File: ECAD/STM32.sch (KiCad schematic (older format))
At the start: 13 parts, among them J4 Conn_02x03_Odd_Even, U1 STM32F072C8Ux, U2 STM32F071C8Tx

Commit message: routing almost done
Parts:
- removed U2: STM32F071C8Tx, Package_QFP:LQFP-48_7x7mm_P0.5mm, symbol MCU_ST_STM32F0:STM32F071C8Tx
- C2, C3, C4, C7, C8: renamed from C?; symbol Device:C -> OtterIronProRedesign-rescue:C-Device
- C5: renamed from C3; symbol Device:C -> OtterIronProRedesign-rescue:C-Device
- C6: renamed from C4; symbol Device:C -> OtterIronProRedesign-rescue:C-Device
- J23: renamed from J4; symbol Connector_Generic:Conn_02x03_Odd_Even -> OtterIronProRedesign-rescue:Conn_02x03_Odd_Even-Connector_Generic
- NT1: renamed from NT9; symbol Device:Net-Tie_2 -> OtterIronProRedesign-rescue:Net-Tie_2-Device
- NT2: renamed from NT10; symbol Device:Net-Tie_2 -> OtterIronProRedesign-rescue:Net-Tie_2-Device
- R7: renamed from R6; symbol Device:R -> OtterIronProRedesign-rescue:R-Device
- U1: symbol MCU_ST_STM32F0:STM32F072C8Ux -> OtterIronProRedesign-rescue:STM32F072C8Ux-MCU_ST_STM32F0
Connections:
- net CurrentMeasurement: now also U1.11 (PA1); no longer U1.10 (PA0)
- net I2C_SCL: now also U1.21 (PB10); no longer U1.42 (PB6)
- net I2C_SDA: now also U1.22 (PB11); no longer U1.43 (PB7)
- net IronTemperature: now also U1.12 (PA2); no longer U1.11 (PA1)
- net PcbTemperature: now also U1.13 (PA3); no longer U1.15 (PA5)
- net Switch1: now also U1.26 (PB13); no longer U1.13 (PA3)
- net Switch2: now also U1.3 (PC14); no longer U1.2 (PC13)
- net USB_Alert: now also U1.27 (PB14); no longer U1.25 (PB12)
- net VBusMeasurement: now also U1.10 (PA0); no longer U1.12 (PA2)
- net ~VBusAvailable: now also U1.25 (PB12)
- net IronPwmH: now reaches U1.45 (PB8)
- net IronPwm: no longer names the net of U1.29 (PA8)
- new net IronPwmL: U1.42 (PB6)
- no-connect marks 46 -> 21
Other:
- note added: "TIM16_CH1"
- note added: "TIM16_CH1N"

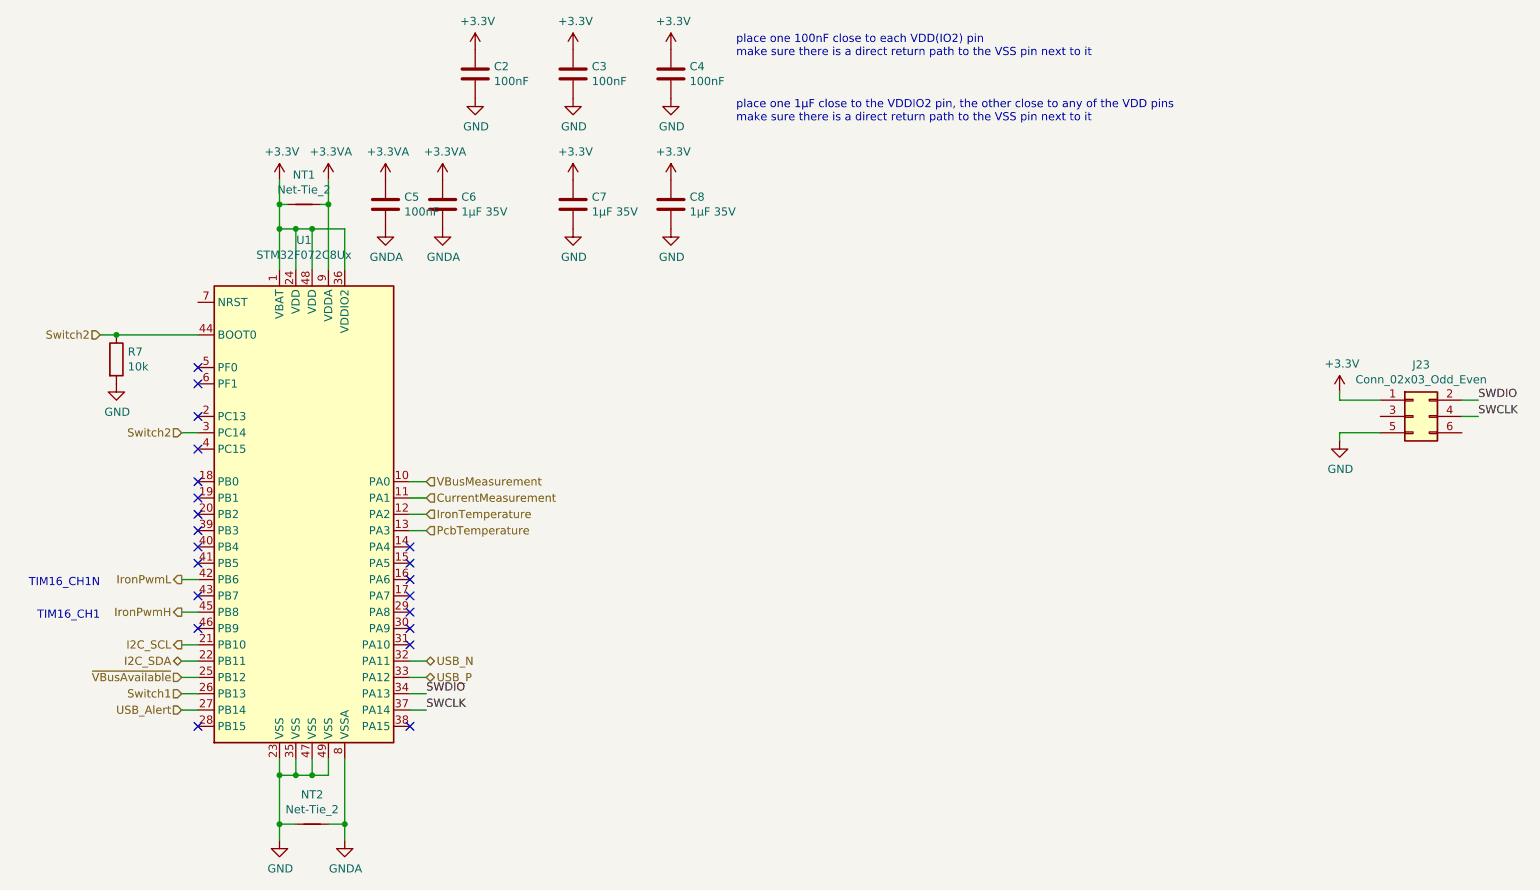
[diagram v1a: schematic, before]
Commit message: swapped microcontroller
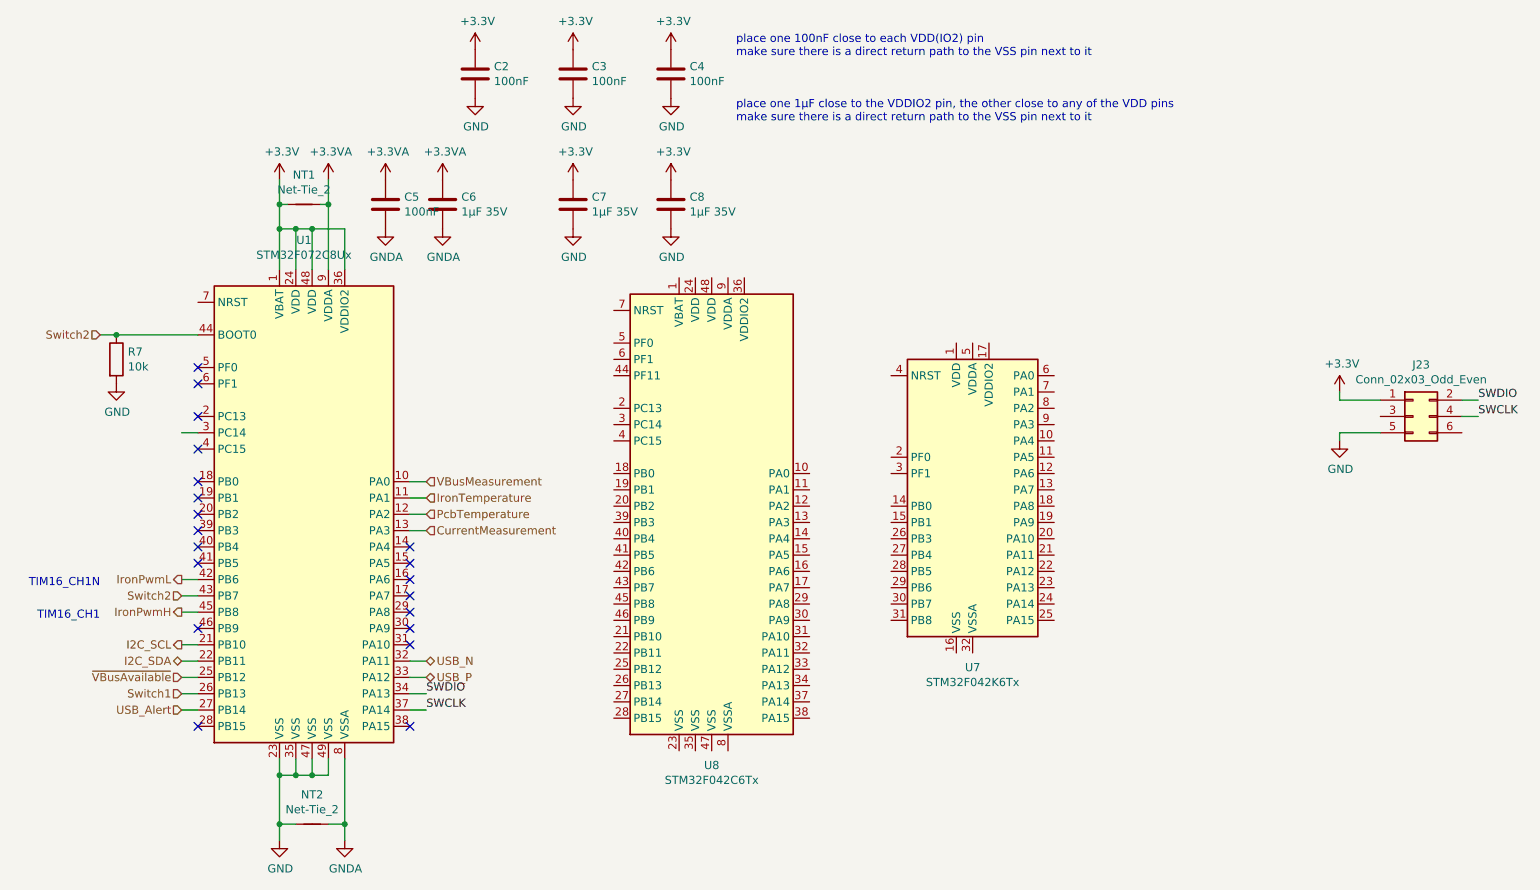
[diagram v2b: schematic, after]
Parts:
- added U7: STM32F042K6Tx, Package_QFP:LQFP-32_7x7mm_P0.8mm, symbol MCU_ST_STM32F0:STM32F042K6Tx
- added U8: STM32F042C6Tx, Package_QFP:LQFP-48_7x7mm_P0.5mm, symbol MCU_ST_STM32F0:STM32F042C6Tx
- NT1, NT2: footprint NetTie:NetTie-2_SMD_Pad0.5mm -> ECAD:NetTie-2_SMD_Pad0.25mm
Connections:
- net CurrentMeasurement: now also U1.13 (PA3); no longer U1.11 (PA1)
- net IronTemperature: now also U1.11 (PA1); no longer U1.12 (PA2)
- net PcbTemperature: now also U1.12 (PA2); no longer U1.13 (PA3)
- net Switch2: now also U1.43 (PB7); no longer U1.3 (PC14)
- no-connect marks 21 -> 20
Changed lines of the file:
@@
 	1    0    0    -1
 $EndComp
+Text HLabel 3000 3700 2    50   Input ~ 0
+CurrentMeasurement
 Text HLabel 3000 3500 2    50   Input ~ 0
-CurrentMeasurement
+IronTemperature
 Text HLabel 3000 3600 2    50   Input ~ 0
-IronTemperature
-Text HLabel 3000 3700 2    50   Input ~ 0
 PcbTemperature
 Text HLabel 3000 4600 2    50   BiDi ~ 0
@@
 F 0 "NT2" H 2300 5681 50  0000 C CNN
 F 1 "Net-Tie_2" H 2300 5590 50  0000 C CNN
-F 2 "NetTie:NetTie-2_SMD_Pad0.5mm" H 2300 5500 50  0001 C CNN
+F 2 "ECAD:NetTie-2_SMD_Pad0.25mm" H 2300 5500 50  0001 C CNN
 F 3 "~" H 2300 5500 50  0001 C CNN
 	1    2300 5500
@@
 NoConn ~ 1600 4900
 NoConn ~ 1600 4300
-NoConn ~ 1600 4100
 NoConn ~ 1600 3400
 NoConn ~ 1600 3500
@@
 F 0 "NT1" H 2250 1881 50  0000 C CNN
 F 1 "Net-Tie_2" H 2250 1790 50  0000 C CNN
-F 2 "NetTie:NetTie-2_SMD_Pad0.5mm" H 2250 1700 50  0001 C CNN
+F 2 "ECAD:NetTie-2_SMD_Pad0.25mm" H 2250 1700 50  0001 C CNN
 F 3 "~" H 2250 1700 50  0001 C CNN
 	1    2250 1700
@@
 	1100 2500 1600 2500
 NoConn ~ 1600 3000
-Text HLabel 1500 3100 0    50   Input ~ 0
+Text HLabel 1500 4100 0    50   Input ~ 0
 Switch2
 Wire Wire Line
 	1500 3100 1600 3100
+Wire Wire Line
+	1500 4100 1600 4100
+$Comp
+L MCU_ST_STM32F0:STM32F042C6Tx U8
+U 1 1 5FC30478
+P 4750 3550
+F 0 "U8" H 4750 1961 50  0000 C CNN
+F 1 "STM32F042C6Tx" H 4750 1870 50  0000 C CNN
+F 2 "Package_QFP:LQFP-48_7x7mm_P0.5mm" H 4250 2150 50  0001 R CNN
+F 3 "http://www.st.com/st-web-ui/static/active/en/resource/technical/document/datasheet/DM00105814.pdf" H 4750 3550 50  0001 C CNN
+	1    4750 3550
+	1    0    0    -1
+$EndComp
+$Comp
+L MCU_ST_STM32F0:STM32F042K6Tx U7
+U 1 1 5FC31F08
+P 6350 3450
+F 0 "U7" H 6350 2361 50  0000 C CNN
+F 1 "STM32F042K6Tx" H 6350 2270 50  0000 C CNN
+F 2 "Package_QFP:LQFP-32_7x7mm_P0.8mm" H 5950 2550 50  0001 R CNN
+F 3 "http://www.st.com/st-web-ui/static/active/en/resource/technical/document/datasheet/DM00105814.pdf" H 6350 3450 50  0001 C CNN
+	1    6350 3450
+	1    0    0    -1
+$EndComp
 $EndSCHEMATC

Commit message: forgot to save
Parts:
- removed C4: 100nF, Capacitor_SMD:C_0402_1005Metric, symbol OtterIronProRedesign-rescue:C-Device
- removed U1: STM32F072C8Ux, Package_DFN_QFN:QFN-48-1EP_7x7mm_P0.5mm_EP5.6x5.6mm, symbol OtterIronProRedesign-rescue:STM32F072C8Ux-MCU_ST_STM32F0
- removed U8: STM32F042C6Tx, Package_QFP:LQFP-48_7x7mm_P0.5mm, symbol MCU_ST_STM32F0:STM32F042C6Tx
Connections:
- wire segments 51 -> 72

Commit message: more routing + some component changes
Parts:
- renumbered C5 to C2, C6 to C3, C2 to C4, C3 to C5, C7 to C6, C8 to C7, J23 to J17, U7 to U1
